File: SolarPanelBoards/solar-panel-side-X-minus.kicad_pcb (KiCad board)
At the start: 2 copper layers, 82 x 99 mm, 24 parts, among them J1 Conn_01x06, U1 OPT3001DNPT

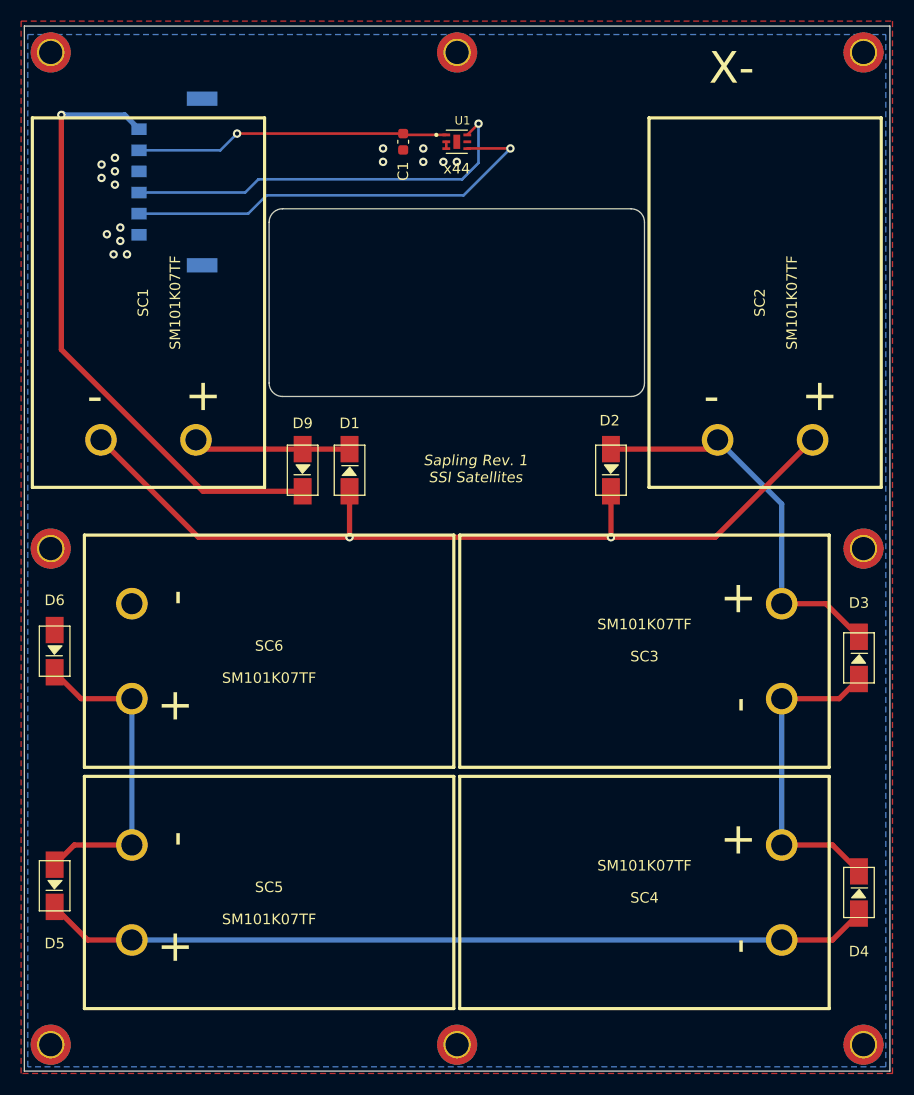
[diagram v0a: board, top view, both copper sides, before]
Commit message: Battery board and side panels ready for CAD check and review, pycubed not finished yet
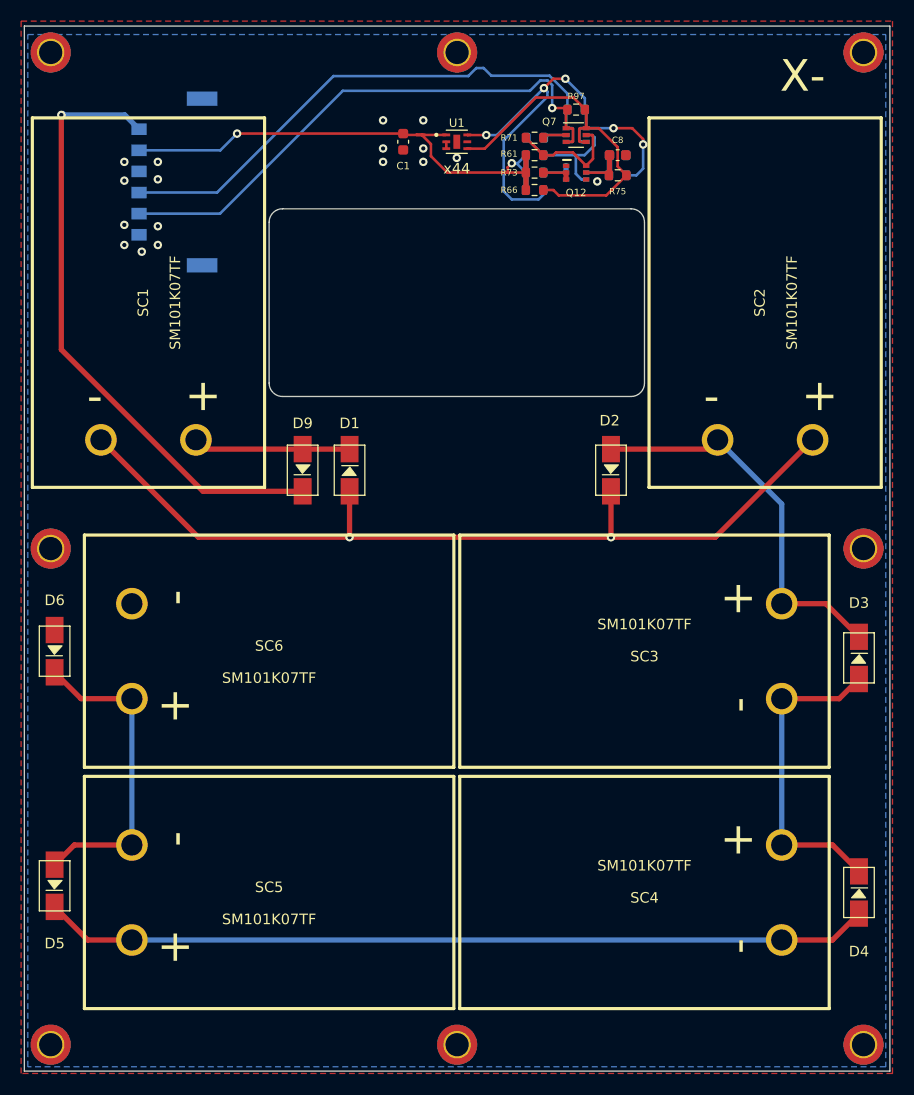
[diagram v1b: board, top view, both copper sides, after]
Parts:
- added C40: 10nF, Capacitor_SMD:C_0603_1608Metric, B.Cu at (166.4, 55.9)
- added C8: 10nF, Capacitor_SMD:C_0603_1608Metric, F.Cu at (166.4, 55.9)
- added Q12: BSS138DWQ-7, sapling:BSS138DWQ-7, F.Cu at (162.4, 57.5)
- added Q13: BSS138DWQ-7, sapling:BSS138DWQ-7, B.Cu at (162.4, 57.5)
- added Q7: MBT2222ADW1T1, Package_TO_SOT_SMD:SOT-363_SC-70-6, F.Cu at (162.4, 54.0)
- added Q8: MBT2222ADW1T1, Package_TO_SOT_SMD:SOT-363_SC-70-6, B.Cu at (162.4, 54.0)
- added R61: 10K, Resistor_SMD:R_0603_1608Metric, F.Cu at (158.5, 55.9)
- added R62: 10K, Resistor_SMD:R_0603_1608Metric, B.Cu at (158.5, 55.9)
- added R66: 10K, Resistor_SMD:R_0603_1608Metric, F.Cu at (158.5, 59.2)
- added R67: 10K, Resistor_SMD:R_0603_1608Metric, B.Cu at (158.5, 59.2)
- added R71: 680, Resistor_SMD:R_0603_1608Metric, F.Cu at (158.5, 54.2)
- added R72: 680, Resistor_SMD:R_0603_1608Metric, B.Cu at (158.6, 54.2)
- added R73: 100K, Resistor_SMD:R_0603_1608Metric, F.Cu at (158.5, 57.5)
- added R74: 100K, Resistor_SMD:R_0603_1608Metric, B.Cu at (158.5, 57.5)
- added R75: 200K, Resistor_SMD:R_0603_1608Metric, F.Cu at (166.4, 57.8)
- added R76: 200K, Resistor_SMD:R_0603_1608Metric, B.Cu at (166.4, 57.8)
- added R97: 0, Resistor_SMD:R_0603_1608Metric, F.Cu at (162.4, 51.6)
- added R98: 0, Resistor_SMD:R_0603_1608Metric, B.Cu at (162.4, 51.6)
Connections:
- U1 pad 4: SCL -> SCL_SUN
- U1 pad 6: SDA -> SDA_SUN
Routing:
- net SDA_SUN: track 0.00 -> 46.3 mm, vias 0 -> 5
- net SCL_SUN: track 0.00 -> 33.6 mm
- net +3V3: track 29.9 -> 53.7 mm, vias 1 -> 2
- net SDA: track 38.6 -> 52.3 mm, vias 1 -> 0
- net Net-(Q13-Pad6): track 0.00 -> 12.2 mm
- net Net-(Q12-Pad6): track 0.00 -> 10.8 mm
- net SCL: track 42.0 -> 52.6 mm
- net Net-(C8-Pad1): track 0.00 -> 4.19 mm
- net Net-(C40-Pad1): track 0.00 -> 4.19 mm
- net Net-(Q13-Pad2): track 0.00 -> 2.81 mm
- net Net-(Q12-Pad2): track 0.00 -> 2.81 mm
- net Net-(Q7-Pad2): track 0.00 -> 2.27 mm
- net Net-(Q8-Pad2): track 0.00 -> 2.20 mm
- net GND: vias 16 -> 17
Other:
- board text removed: "Sapling Rev. 1 SSI Satellites"

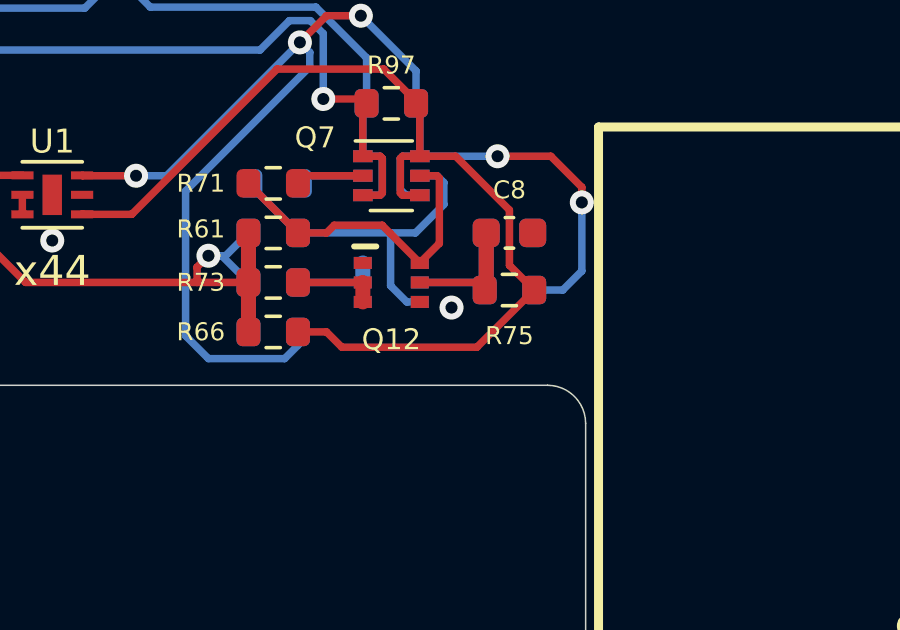
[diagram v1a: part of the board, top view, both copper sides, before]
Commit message: side panels ready except for RF trace width
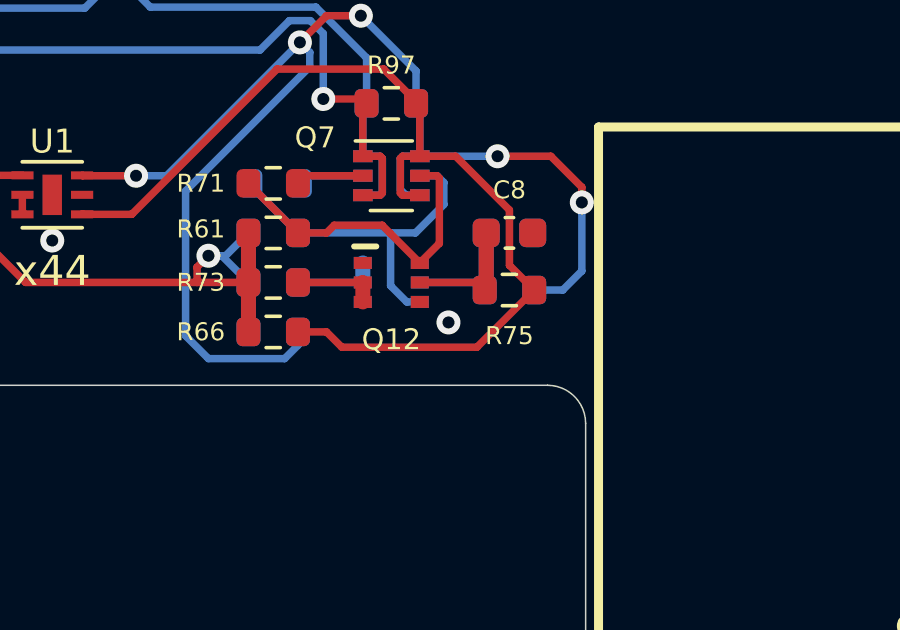
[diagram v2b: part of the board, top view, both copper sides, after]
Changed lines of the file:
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@@
   (via (at 144.145 56.515) (size 0.8) (drill 0.4) (layers F.Cu B.Cu) (net 7))
   (via (at 147.955 56.515) (size 0.8) (drill 0.4) (layers F.Cu B.Cu) (net 7))
-  (via (at 164.4396 58.3692) (size 0.8) (drill 0.4) (layers F.Cu B.Cu) (net 7))
+  (via (at 164.338 58.8645) (size 0.8) (drill 0.4) (layers F.Cu B.Cu) (net 7))
   (via (at 147.955 52.578) (size 0.8) (drill 0.4) (layers F.Cu B.Cu) (net 7))
   (via (at 144.145 52.578) (size 0.8) (drill 0.4) (layers F.Cu B.Cu) (net 7))
